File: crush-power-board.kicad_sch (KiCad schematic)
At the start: 8 parts

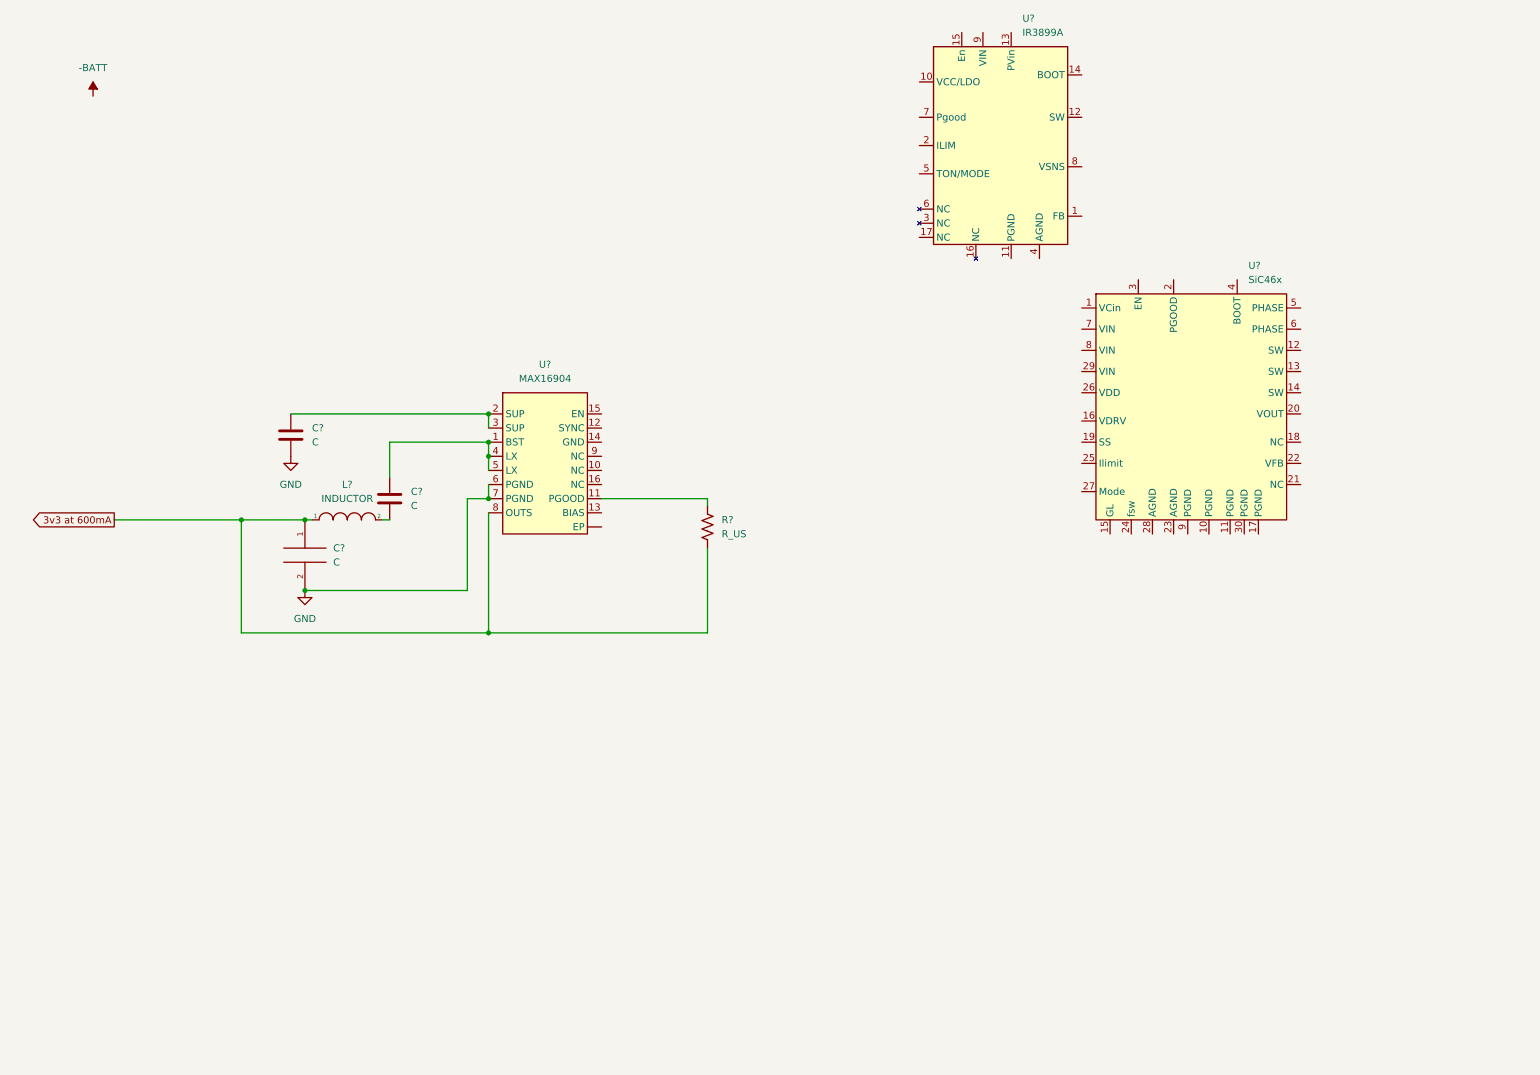
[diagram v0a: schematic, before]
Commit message: added all power regulator circuits
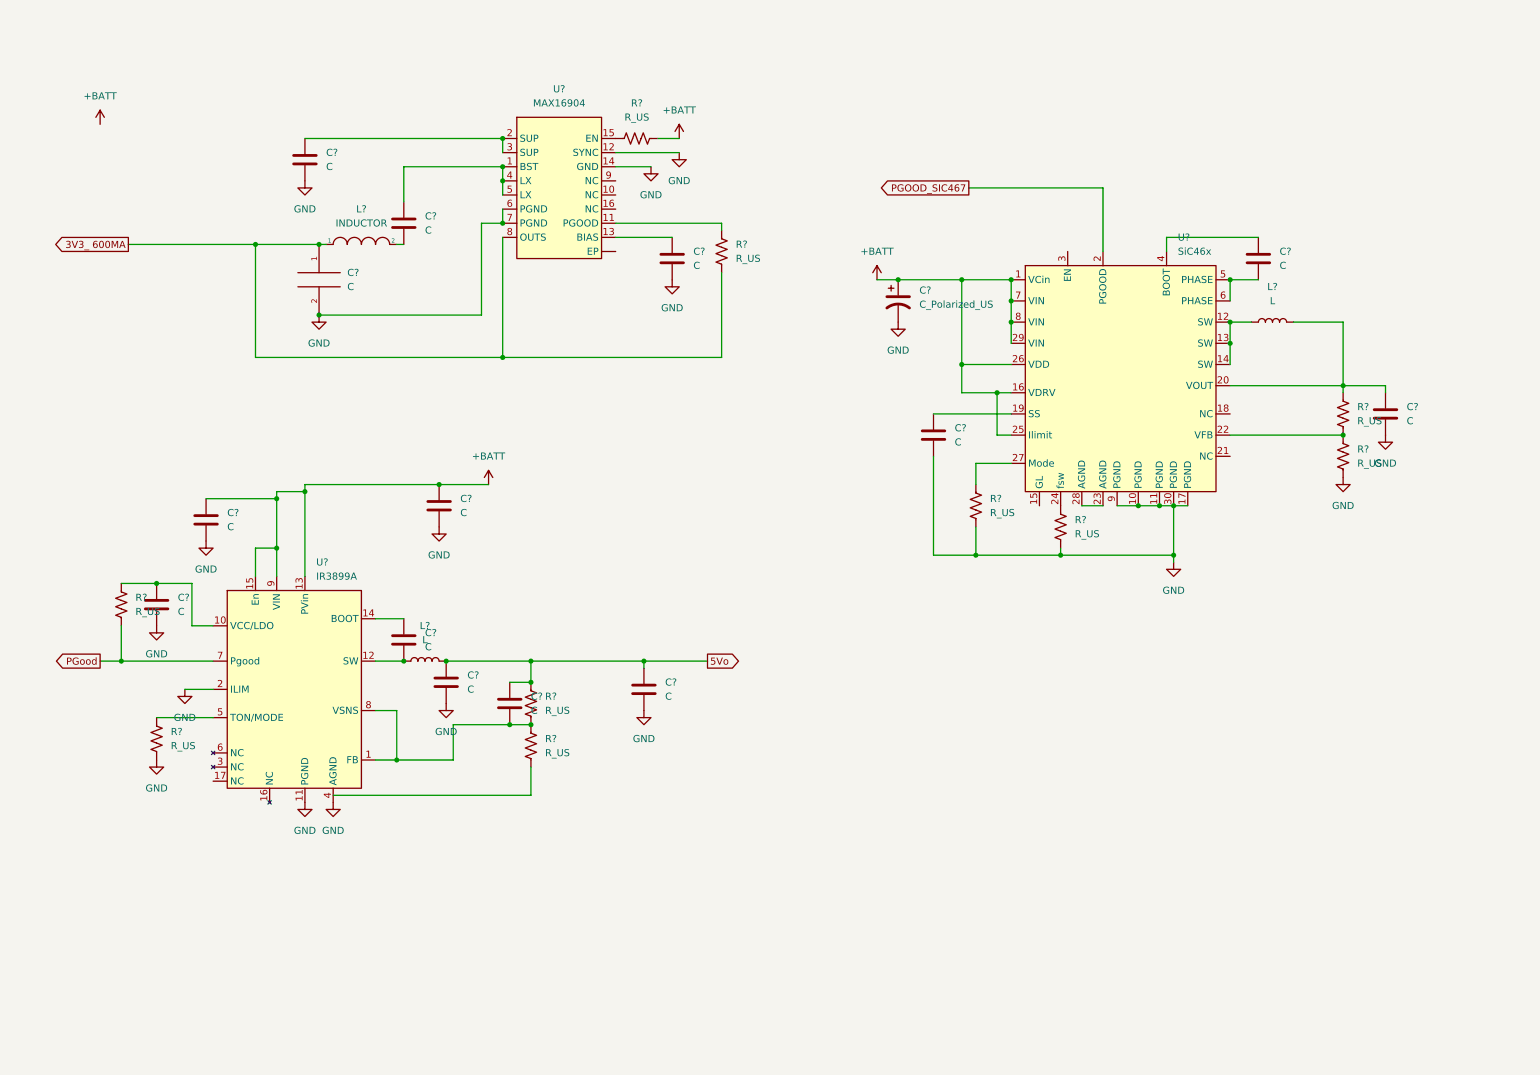
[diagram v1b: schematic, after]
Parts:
- added C? (x11): C, symbol Device:C
- added C?: C_Polarized_US, symbol Device:C_Polarized_US
- added L? (x2): L, symbol Device:L
- added R? (x9): R_US, symbol Device:R_US
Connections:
- net GND: now also U?.10 (PGND), U?.11 (PGND), U?.11 (PGND), U?.12 (SYNC), U?.14 (GND), U?.17 (PGND), U?.2 (ILIM), U?.30 (PGND), U?.4 (AGND), U?.9 (PGND), C?.2, C?.2, C?.2, C?.2, C?.2, C?.2, C?.2, C?.2, C?.2, R?.2, R?.2, R?.2, R?.2
- net +BATT: now reaches U?.1 (VCin)
- net +BATT: now also U?.13 (PVin), U?.15 (En), U?.16 (VDRV), U?.25 (Ilimit), U?.26 (VDD), U?.29 (VIN), U?.7 (VIN), U?.8 (VIN), U?.9 (VIN), C?.1, C?.1, C?.1, R?.2
- net at U?.12 (SW): now also U?.13 (SW), U?.14 (SW), L?.1
- net at U?.19 (SS): now also C?.1
- net PGOOD_SIC467: now reaches U?.2 (PGOOD)
- net at U?.20 (VOUT): now also C?.1, L?.2, R?.1
- net at U?.22 (VFB): now also R?.1, R?.2
- net at U?.23 (AGND): now also U?.28 (AGND)
- net at U?.24 (fsw): now also R?.1
- net at U?.27 (Mode): now also R?.1
- net at U?.4 (BOOT): now also C?.1
- net at U?.5 (PHASE): now also U?.6 (PHASE), C?.2
- net at U?.1 (FB): now also U?.8 (VSNS), C?.2, R?.1, R?.2
- net at U?.10 (VCC/LDO): now also C?.1, R?.1
- net at U?.12 (SW): now also C?.2, L?.1
- net at U?.14 (BOOT): now also C?.1
- net at U?.5 (TON/MODE): now also R?.1
- net PGood: now reaches U?.7 (Pgood)
- net PGood: now also R?.2
- net at U?.13 (BIAS): now also C?.1
- net at U?.15 (EN): now also R?.1
- net 3v3 at 600mA renamed 3V3_ 600MA
- new net 5Vo: C?.1, C?.1, C?.1, L?.2, R?.1
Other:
- moved on the sheet: C?, L?, R?, U?

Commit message: Added component values for the 3V3 regulator, cleaned up some schematics
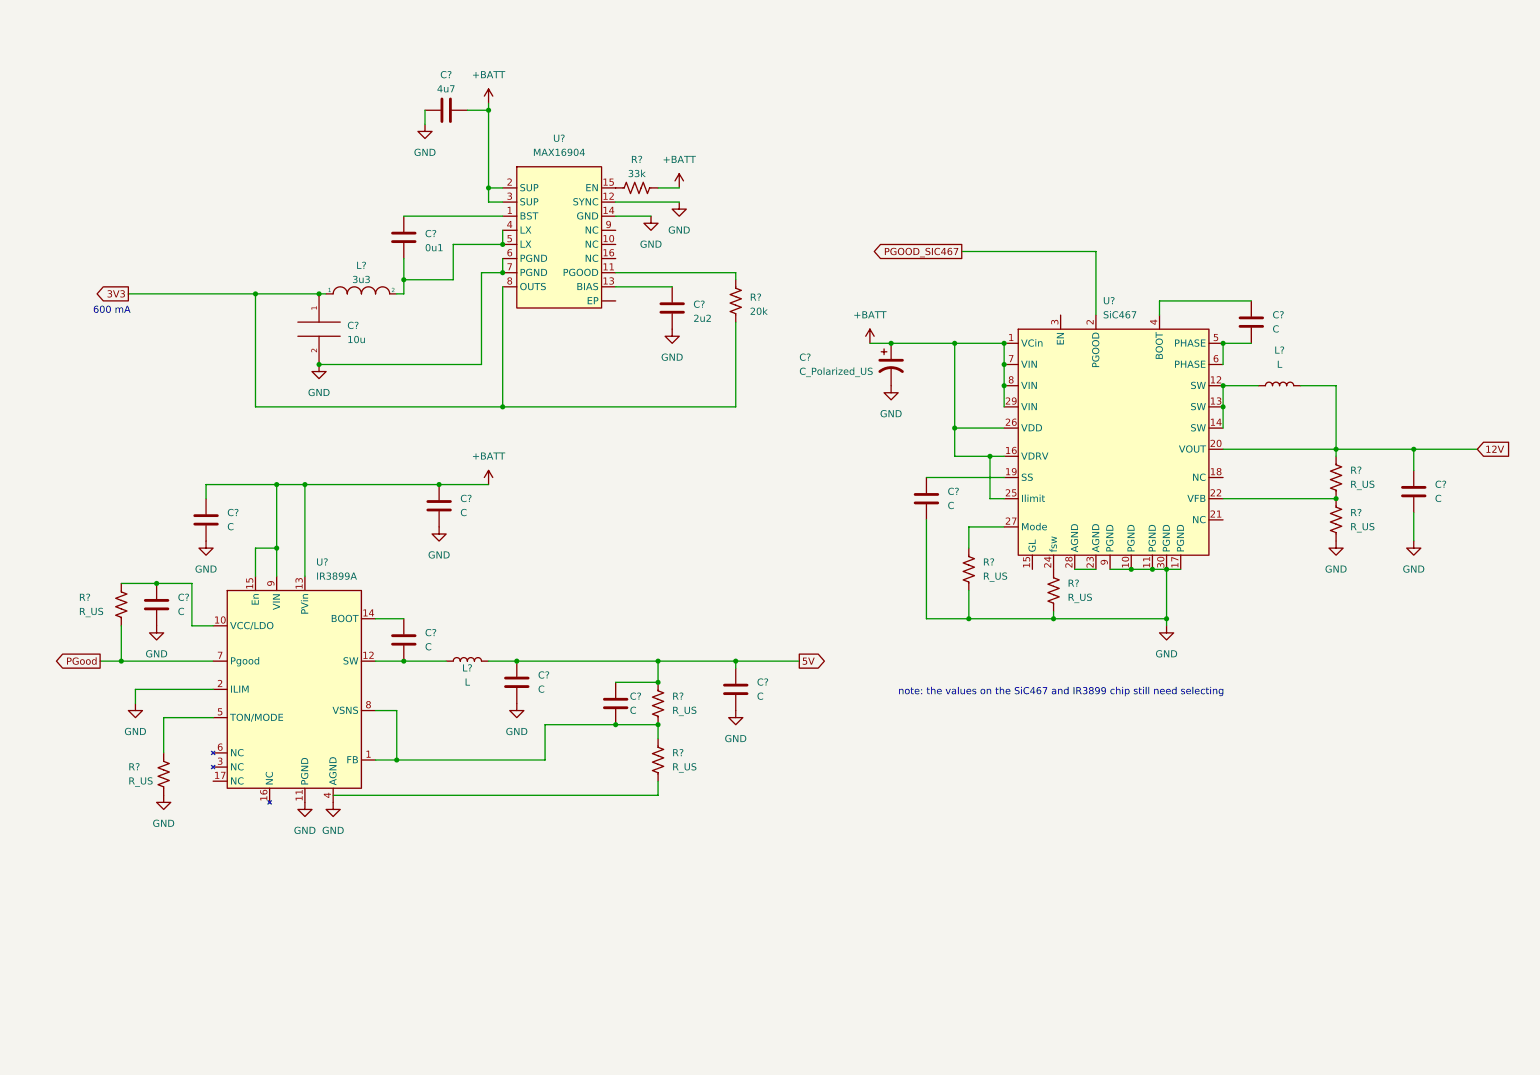
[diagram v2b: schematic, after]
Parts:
- C?: value C -> 0u1
- C?: value C -> 10u
- C?: value C -> 2u2
- C?: value C -> 4u7
- L?: value INDUCTOR -> 3u3
- R?: value R_US -> 33k
- R?: value R_US -> 20k
- U?: value SiC46x -> SiC467
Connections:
- net +BATT: now also C?.1, U?.2 (SUP), U?.3 (SUP)
- net 12V: now reaches C?.1, L?.2, R?.1, U?.20 (VOUT)
- net at C?.1, L?.2: now also U?.4 (LX), U?.5 (LX)
- net at C?.2, U?.1 (BST): no longer U?.4 (LX), U?.5 (LX)
- net 3V3_ 600MA renamed 3V3
- net 5Vo renamed 5V
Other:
- note added: "600 mA"
- note added: "note: the values on the SiC467 and IR3899 chip still need selecting"
- moved on the sheet: C?, L?, R?, U?

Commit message: Added values to components
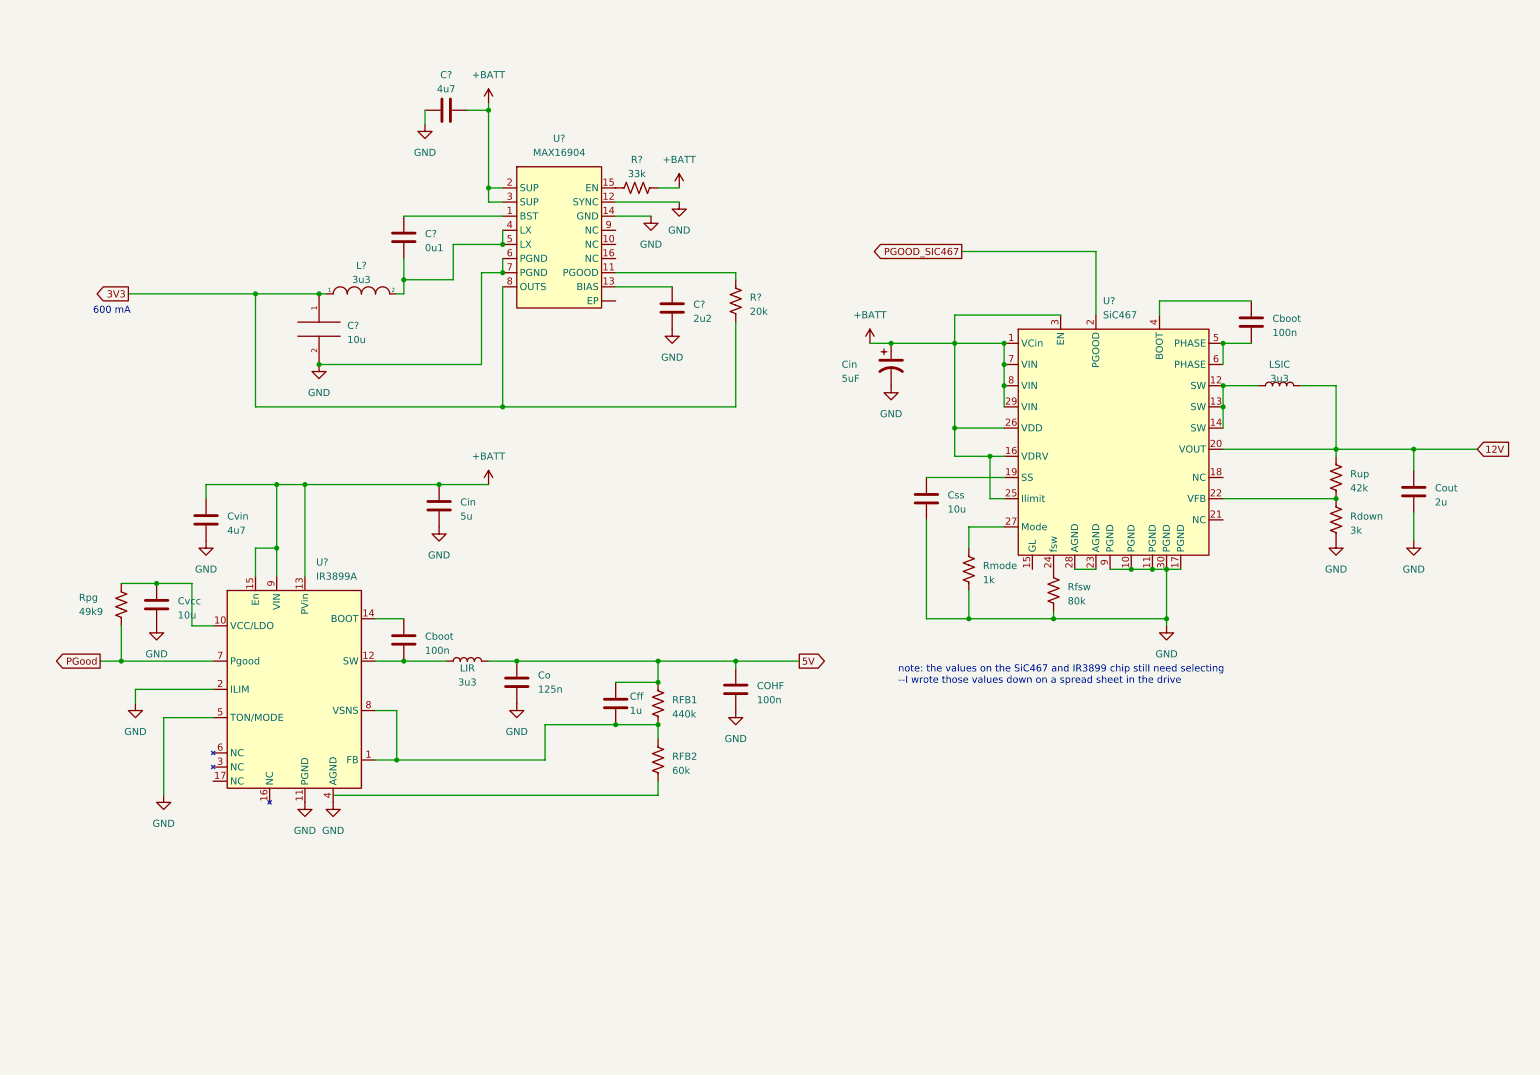
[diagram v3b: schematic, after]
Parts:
- removed R?: R_US, symbol Device:R_US
- COHF, Cboot: renamed from C?; value C -> 100n
- Cff: renamed from C?; value C -> 1u
- Cin: renamed from C?; value C_Polarized_US -> 5uF
- Cin: renamed from C?; value C -> 5u
- Co: renamed from C?; value C -> 125n
- Cout: renamed from C?; value C -> 2u
- Css, Cvcc: renamed from C?; value C -> 10u
- Cvin: renamed from C?; value C -> 4u7
- LIR, LSIC: renamed from L?; value L -> 3u3
- RFB1: renamed from R?; value R_US -> 440k
- RFB2: renamed from R?; value R_US -> 60k
- Rdown: renamed from R?; value R_US -> 3k
- Rfsw: renamed from R?; value R_US -> 80k
- Rmode: renamed from R?; value R_US -> 1k
- Rpg: renamed from R?; value R_US -> 49k9
- Rup: renamed from R?; value R_US -> 42k
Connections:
- net +BATT: now also U?.3 (EN)
- net GND: now also U?.5 (TON/MODE)
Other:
- note added: "note: the values on the SiC467 and IR3899 chip still need selecting --I wrote those values down on a spread sheet in the drive"
- note removed: "note: the values on the SiC467 and IR3899 chip still need selecting"

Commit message: Changed 3.3V Regulator, as well as added hierarchical elements to schematic
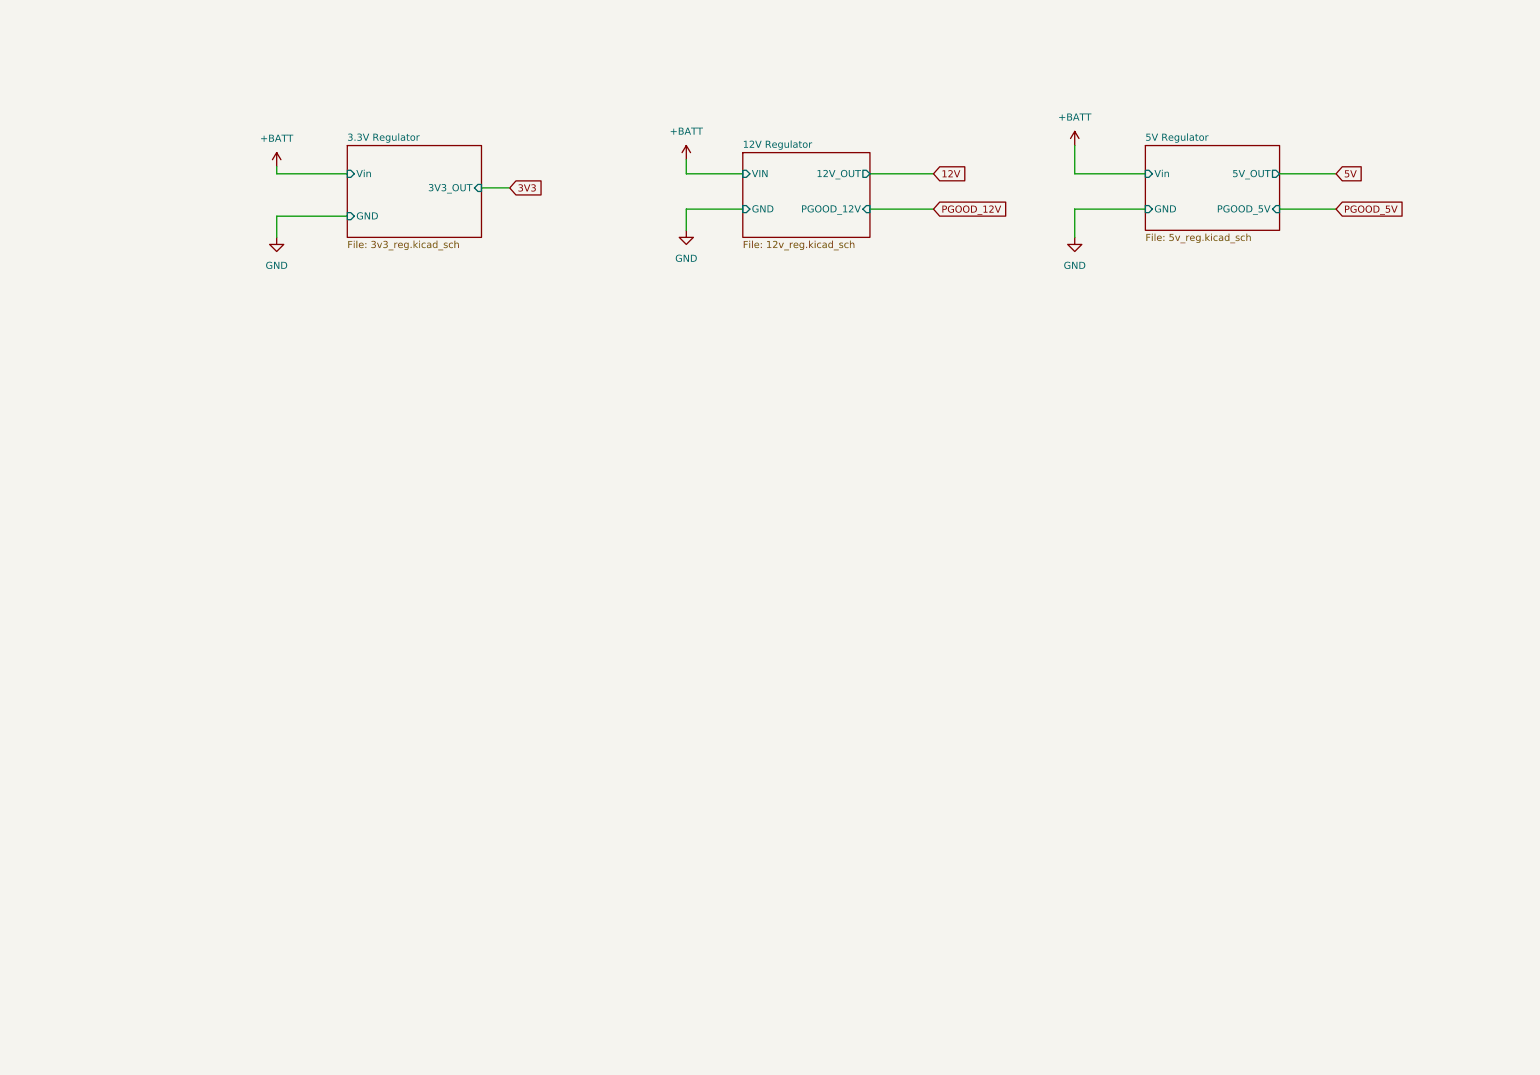
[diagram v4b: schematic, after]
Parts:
- removed C?: 0u1, symbol Device:C
- removed C?: 10u, symbol pspice:C
- removed C?: 2u2, symbol Device:C
- removed C?, Cvin: 4u7, symbol Device:C
- removed COHF, Cboot (x2): 100n, symbol Device:C
- removed Cff: 1u, symbol Device:C
- removed Cin: 5uF, symbol Device:C_Polarized_US
- removed Cin: 5u, symbol Device:C
- removed Co: 125n, symbol Device:C
- removed Cout: 2u, symbol Device:C
- removed Css, Cvcc: 10u, symbol Device:C
- removed L?: 3u3, symbol pspice:INDUCTOR
- removed LIR, LSIC: 3u3, symbol Device:L
- removed R?: 33k, symbol Device:R_US
- removed R?: 20k, symbol Device:R_US
- removed RFB1: 440k, symbol Device:R_US
- removed RFB2: 60k, symbol Device:R_US
- removed Rdown: 3k, symbol Device:R_US
- removed Rfsw: 80k, symbol Device:R_US
- removed Rmode: 1k, symbol Device:R_US
- removed Rpg: 49k9, symbol Device:R_US
- removed Rup: 42k, symbol Device:R_US
- removed U?: SiC467, symbol MuddSubPowerReg:SiC46x
- removed U?: IR3899A, symbol MuddSubPowerReg:IR3899A
- removed U?: MAX16904, symbol MuddSubPowerReg:MAX16904
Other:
- added sheet 12V Regulator (12v_reg.kicad_sch)
- added sheet 3.3V Regulator (3v3_reg.kicad_sch)
- added sheet 5V Regulator (5v_reg.kicad_sch)
- note removed: "600 mA"
- note removed: "note: the values on the SiC467 and IR3899 chip still need selecting --I wrote those values down on a spread sheet in the drive"
